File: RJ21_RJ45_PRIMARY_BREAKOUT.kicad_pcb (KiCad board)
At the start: 2 copper layers, 120 x 120 mm, 21 parts, among them J1 RJ45, J10 RJ45, J11 RJ45, J12 RJ45, J13 RJ45, J14 RJ45, J15 RJ45, J16 RJ45, J17 RJ21 Connector, J2 RJ45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

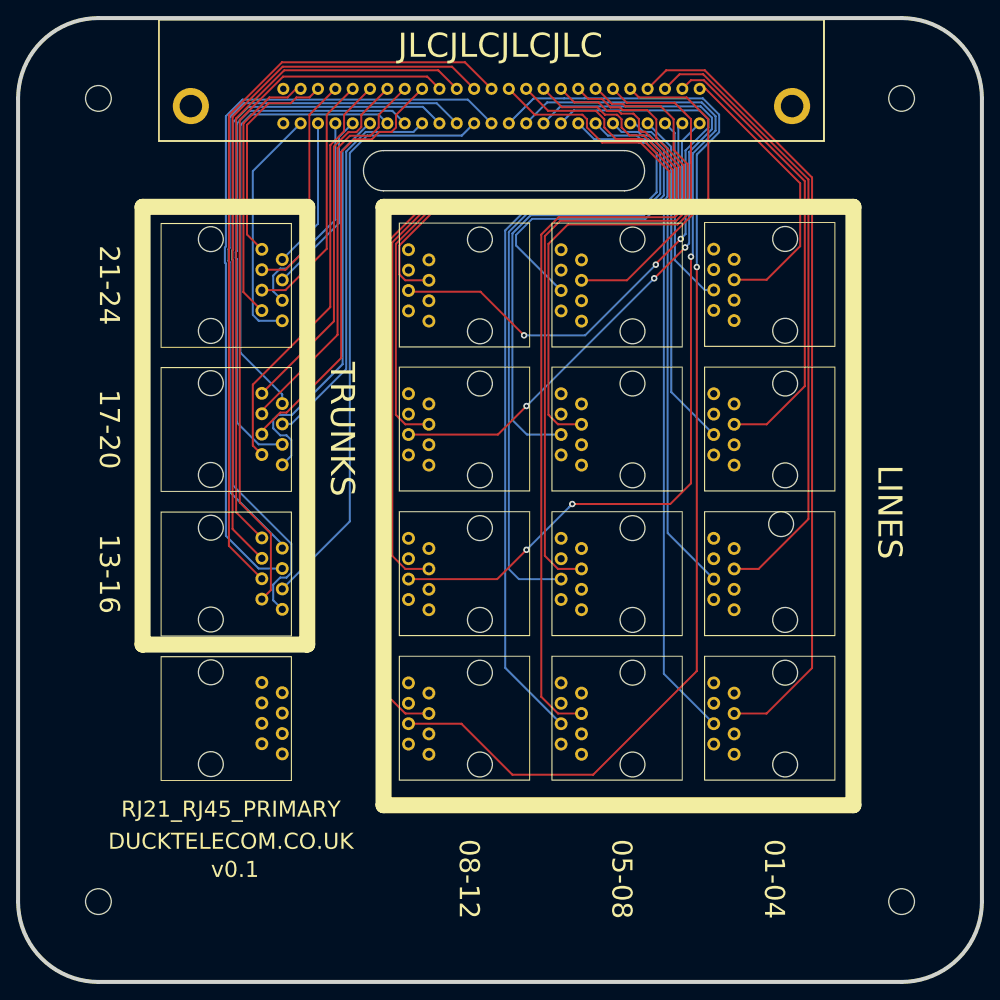
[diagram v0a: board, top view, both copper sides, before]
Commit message: Fix silk screen, re-align J3, remove J16
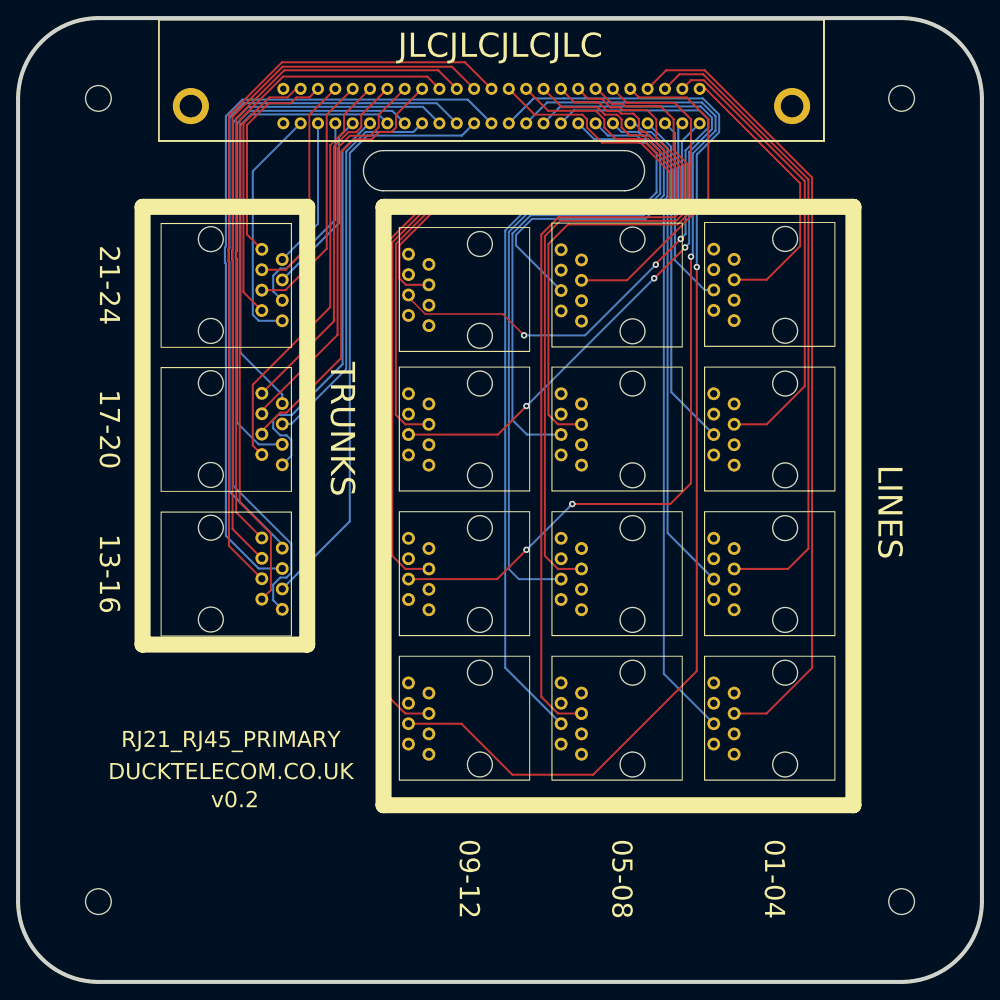
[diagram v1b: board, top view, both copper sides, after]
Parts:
- removed J16: RJ45, Ali_Footprint_Libraries:AliExpress_Horizontal_RJ45
- moved J9 0.56 mm to (155.2, 83.8)
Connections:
- J1 pad 1: Net-(J1-Pad1) -> unconnected-(J1-Pad1)
- J1 pad 2: Net-(J1-Pad2) -> unconnected-(J1-Pad2)
- J1 pad 3: Net-(J1-Pad3) -> unconnected-(J1-Pad3)
- J1 pad 6: Net-(J1-Pad6) -> unconnected-(J1-Pad6)
- J1 pad 7: Net-(J1-Pad7) -> unconnected-(J1-Pad7)
- J1 pad 8: Net-(J1-Pad8) -> unconnected-(J1-Pad8)
- J10 pad 1: Net-(J10-Pad1) -> unconnected-(J10-Pad1)
- J10 pad 2: Net-(J10-Pad2) -> unconnected-(J10-Pad2)
- J10 pad 3: Net-(J10-Pad3) -> unconnected-(J10-Pad3)
- J10 pad 6: Net-(J10-Pad6) -> unconnected-(J10-Pad6)
- J10 pad 7: Net-(J10-Pad7) -> unconnected-(J10-Pad7)
- J10 pad 8: Net-(J10-Pad8) -> unconnected-(J10-Pad8)
- J11 pad 1: Net-(J11-Pad1) -> unconnected-(J11-Pad1)
- J11 pad 2: Net-(J11-Pad2) -> unconnected-(J11-Pad2)
- J11 pad 3: Net-(J11-Pad3) -> unconnected-(J11-Pad3)
- J11 pad 6: Net-(J11-Pad6) -> unconnected-(J11-Pad6)
- J11 pad 7: Net-(J11-Pad7) -> unconnected-(J11-Pad7)
- J11 pad 8: Net-(J11-Pad8) -> unconnected-(J11-Pad8)
- J12 pad 1: Net-(J12-Pad1) -> unconnected-(J12-Pad1)
- J12 pad 2: Net-(J12-Pad2) -> unconnected-(J12-Pad2)
- J12 pad 3: Net-(J12-Pad3) -> unconnected-(J12-Pad3)
- J12 pad 6: Net-(J12-Pad6) -> unconnected-(J12-Pad6)
- J12 pad 7: Net-(J12-Pad7) -> unconnected-(J12-Pad7)
- J12 pad 8: Net-(J12-Pad8) -> unconnected-(J12-Pad8)
- J17 pad 25: Net-(J17-Pad25) -> unconnected-(J17-Pad25)
- J17 pad 50: Net-(J17-Pad50) -> unconnected-(J17-Pad50)
- J2 pad 1: Net-(J2-Pad1) -> unconnected-(J2-Pad1)
- J2 pad 2: Net-(J2-Pad2) -> unconnected-(J2-Pad2)
- J2 pad 3: Net-(J2-Pad3) -> unconnected-(J2-Pad3)
- J2 pad 6: Net-(J2-Pad6) -> unconnected-(J2-Pad6)
- J2 pad 7: Net-(J2-Pad7) -> unconnected-(J2-Pad7)
- J2 pad 8: Net-(J2-Pad8) -> unconnected-(J2-Pad8)
- J3 pad 1: Net-(J3-Pad1) -> unconnected-(J3-Pad1)
- J3 pad 2: Net-(J3-Pad2) -> unconnected-(J3-Pad2)
- J3 pad 3: Net-(J3-Pad3) -> unconnected-(J3-Pad3)
- J3 pad 6: Net-(J3-Pad6) -> unconnected-(J3-Pad6)
- J3 pad 7: Net-(J3-Pad7) -> unconnected-(J3-Pad7)
- J3 pad 8: Net-(J3-Pad8) -> unconnected-(J3-Pad8)
- J4 pad 1: Net-(J4-Pad1) -> unconnected-(J4-Pad1)
- J4 pad 2: Net-(J4-Pad2) -> unconnected-(J4-Pad2)
- J4 pad 3: Net-(J4-Pad3) -> unconnected-(J4-Pad3)
- J4 pad 6: Net-(J4-Pad6) -> unconnected-(J4-Pad6)
- J4 pad 7: Net-(J4-Pad7) -> unconnected-(J4-Pad7)
- J4 pad 8: Net-(J4-Pad8) -> unconnected-(J4-Pad8)
- J5 pad 1: Net-(J5-Pad1) -> unconnected-(J5-Pad1)
- J5 pad 2: Net-(J5-Pad2) -> unconnected-(J5-Pad2)
- J5 pad 3: Net-(J5-Pad3) -> unconnected-(J5-Pad3)
- J5 pad 6: Net-(J5-Pad6) -> unconnected-(J5-Pad6)
- J5 pad 7: Net-(J5-Pad7) -> unconnected-(J5-Pad7)
- J5 pad 8: Net-(J5-Pad8) -> unconnected-(J5-Pad8)
- J6 pad 1: Net-(J6-Pad1) -> unconnected-(J6-Pad1)
- J6 pad 2: Net-(J6-Pad2) -> unconnected-(J6-Pad2)
- J6 pad 3: Net-(J6-Pad3) -> unconnected-(J6-Pad3)
- J6 pad 6: Net-(J6-Pad6) -> unconnected-(J6-Pad6)
- J6 pad 7: Net-(J6-Pad7) -> unconnected-(J6-Pad7)
- J6 pad 8: Net-(J6-Pad8) -> unconnected-(J6-Pad8)
- J7 pad 1: Net-(J7-Pad1) -> unconnected-(J7-Pad1)
- J7 pad 2: Net-(J7-Pad2) -> unconnected-(J7-Pad2)
- J7 pad 3: Net-(J7-Pad3) -> unconnected-(J7-Pad3)
- J7 pad 6: Net-(J7-Pad6) -> unconnected-(J7-Pad6)
- J7 pad 7: Net-(J7-Pad7) -> unconnected-(J7-Pad7)
- J7 pad 8: Net-(J7-Pad8) -> unconnected-(J7-Pad8)
- J8 pad 1: Net-(J8-Pad1) -> unconnected-(J8-Pad1)
- J8 pad 2: Net-(J8-Pad2) -> unconnected-(J8-Pad2)
- J8 pad 3: Net-(J8-Pad3) -> unconnected-(J8-Pad3)
- J8 pad 6: Net-(J8-Pad6) -> unconnected-(J8-Pad6)
- J8 pad 7: Net-(J8-Pad7) -> unconnected-(J8-Pad7)
- J8 pad 8: Net-(J8-Pad8) -> unconnected-(J8-Pad8)
- J9 pad 1: Net-(J9-Pad1) -> unconnected-(J9-Pad1)
- J9 pad 2: Net-(J9-Pad2) -> unconnected-(J9-Pad2)
- J9 pad 3: Net-(J9-Pad3) -> unconnected-(J9-Pad3)
- J9 pad 6: Net-(J9-Pad6) -> unconnected-(J9-Pad6)
- J9 pad 7: Net-(J9-Pad7) -> unconnected-(J9-Pad7)
- J9 pad 8: Net-(J9-Pad8) -> unconnected-(J9-Pad8)
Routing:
- net /L3+: track 78.1 -> 80.3 mm
- net /L9+: track 69.1 -> 69.7 mm
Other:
- net class Default removed
- board text added: "09-12"
- board text added: "v0.2"
- board text removed: "08-12"
- board text removed: "v0.1"

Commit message: Update silkscreen
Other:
- board text added: "RJ21_RJ45_PRIMARY v0.2"
- board text removed: "DUCKTELECOM.CO.UK"
- board text removed: "RJ21_RJ45_PRIMARY"
- board text removed: "v0.2"
